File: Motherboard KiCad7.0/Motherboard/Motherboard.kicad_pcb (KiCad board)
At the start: 2 copper layers, 83.8 x 83.8 mm, 95 parts, among them J1 USB_B_Micro, J10 430450200, J11 430450200, J12 430450200, J2 SWD_01x04_Pin, J3 430450200, J4 430450200, J5 B04B-XASK-1, J6 430450200, J7 430450200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

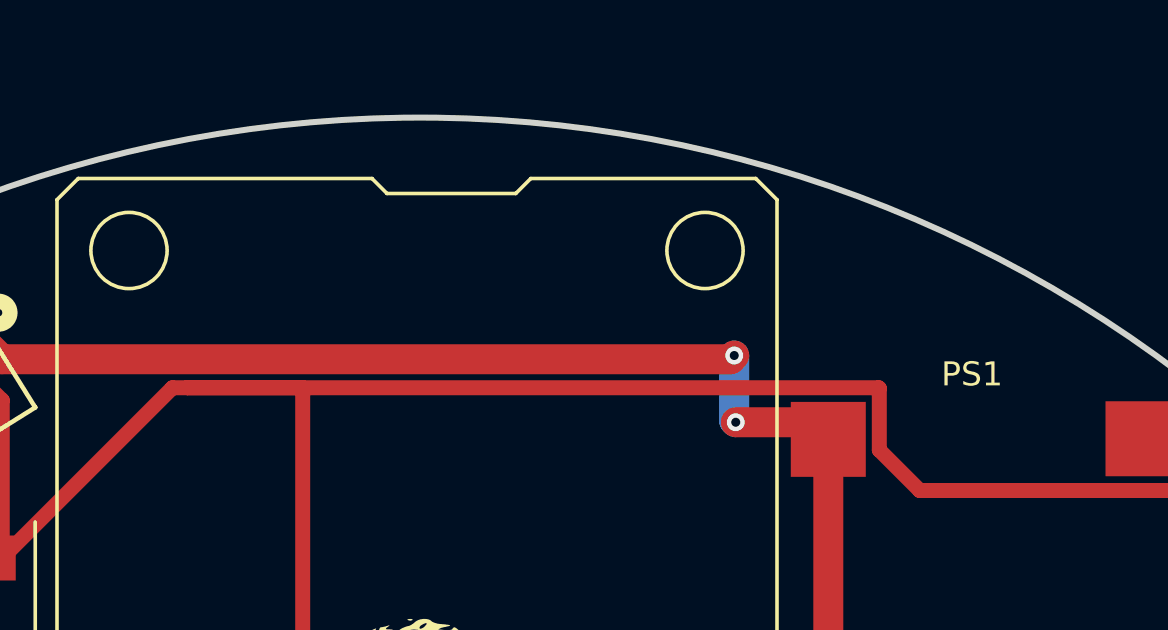
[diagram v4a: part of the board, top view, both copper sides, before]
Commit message: Added power LED
Added power LED and part number for I2C PU resistors
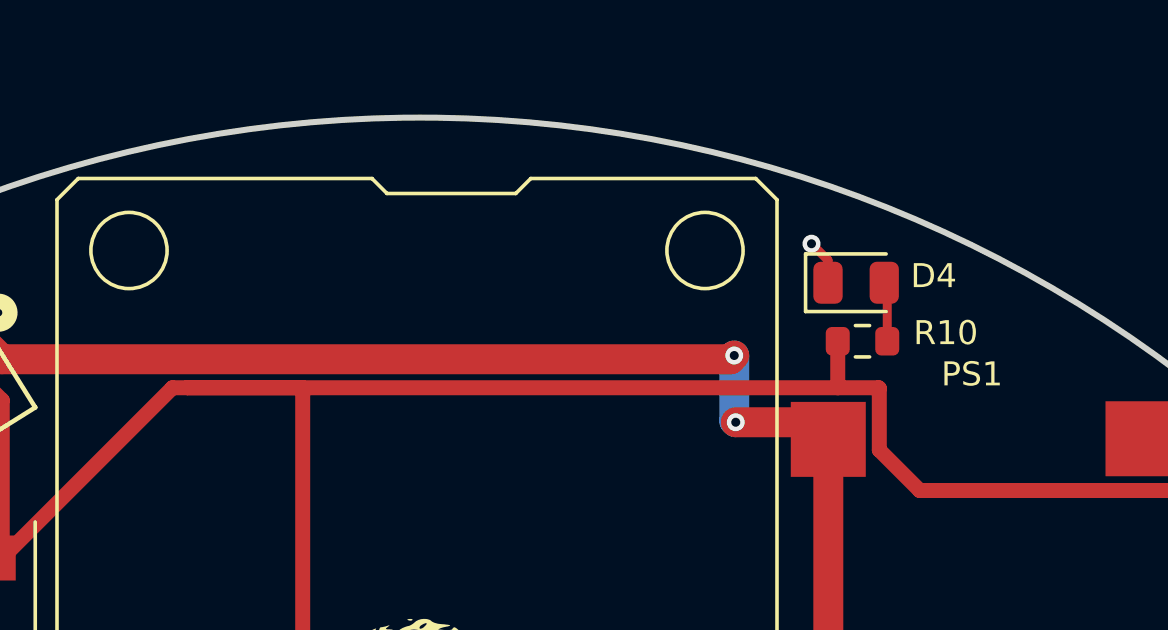
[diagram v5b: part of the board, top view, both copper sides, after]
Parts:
- added D4: 3.3V_A PWR (GRN), LED_SMD:LED_0805_2012Metric, F.Cu at (206.6, 86.5)
- added R10: 1.2k, Resistor_SMD:R_0603_1608Metric, F.Cu at (206.8, 88.5)
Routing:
- net Net-(D4-A): track 0.00 -> 1.99 mm
- net +3.3V: track 400.2 -> 401.8 mm
- net GND: track 180.6 -> 182.1 mm, vias 58 -> 59
